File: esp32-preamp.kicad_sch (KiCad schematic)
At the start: 51 parts, among them J1 PWR IN, J10 TSOP382, J11 SELECT, J2 OUT, J3 LFE, J4 INPUT 1, J5 INPUT 2, J6 INPUT 2, J7 AMP PWR, J8 POT MOTOR, J9 VOLUME, Q1 2N3904, Q2 2N3904, Q3 2N3904, Q4 2N3904, U1 ESP32 D1 Mini, U2 TSR0.5-2450, U3 TPS60402DBV, U4 TPS72301DBV

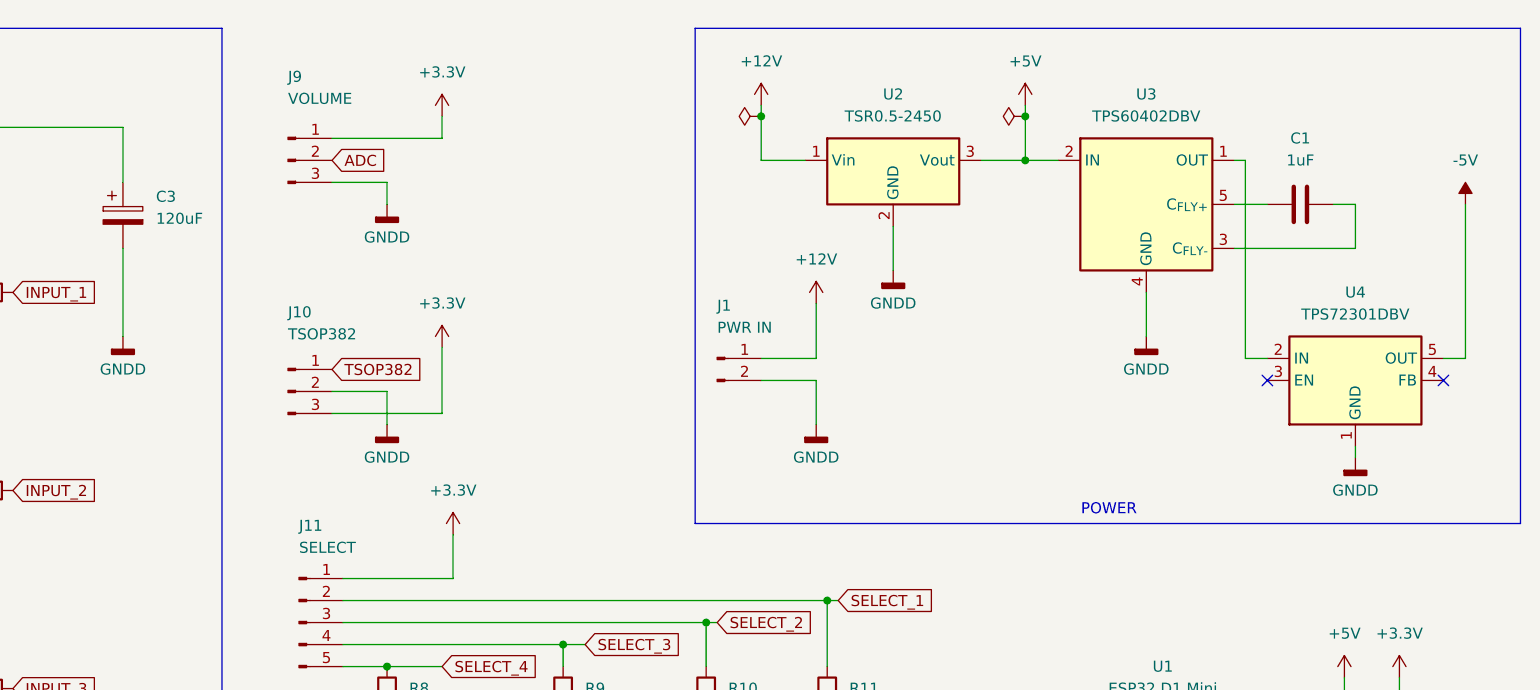
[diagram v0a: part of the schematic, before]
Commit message: Add caps on LDO
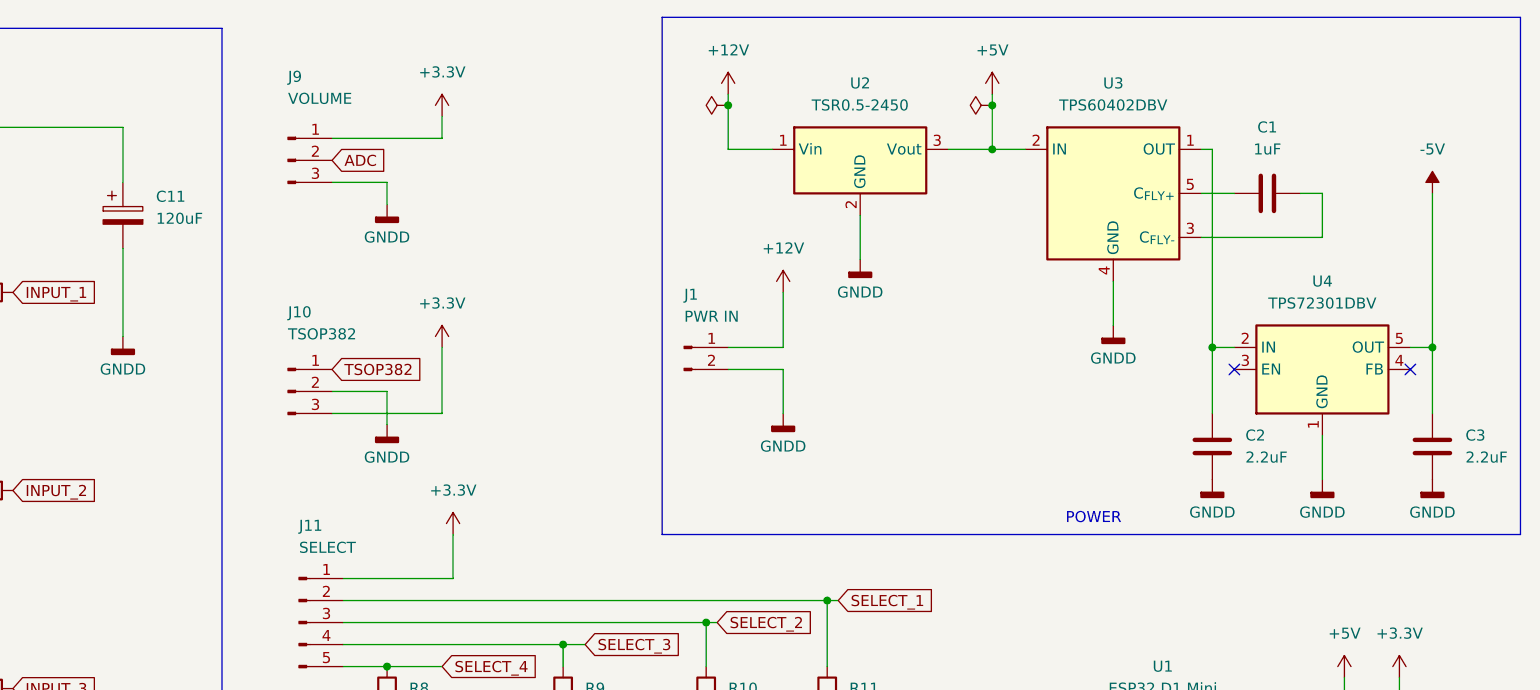
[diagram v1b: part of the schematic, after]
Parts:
- added C2, C3: 2.2uF, symbol Device:C
- renumbered C3 to C11
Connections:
- net -5V: now also C3.1
- net GNDD: now also C3.2
- net at U3.1 (OUT), U4.2 (IN): now also C2.1
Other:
- moved on the sheet: C1, J1, U2, U3, U4

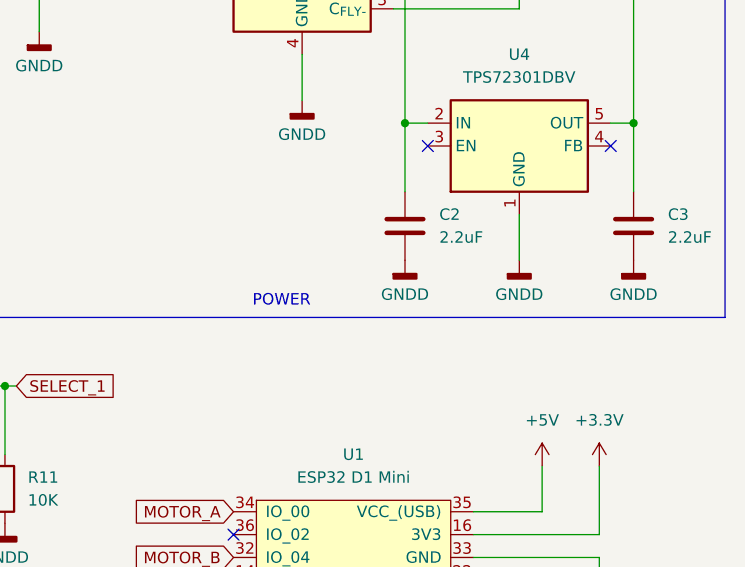
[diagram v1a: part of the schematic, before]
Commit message: Update esp32-preamp.kicad_sch
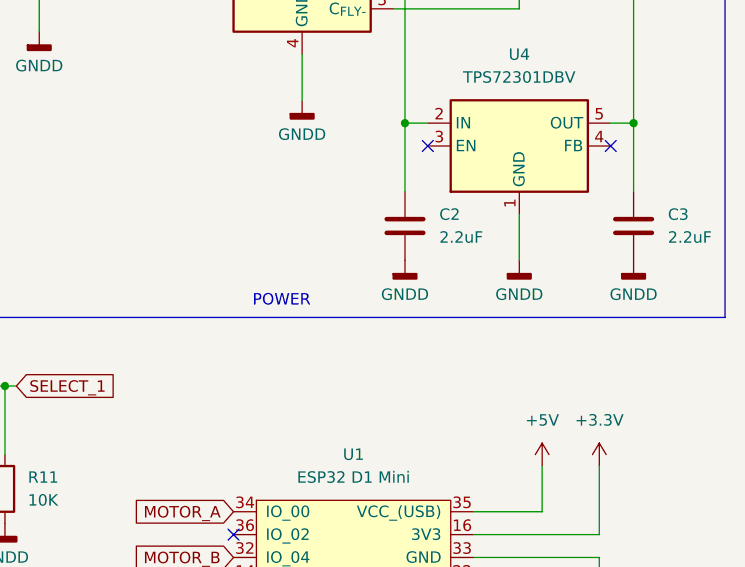
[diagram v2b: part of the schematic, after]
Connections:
- net GNDD: now also C2.2
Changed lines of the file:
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@@
 	(symbol
 		(lib_id "power:GNDD")
-		(at 247.65 67.3042 0)
+		(at 247.65 67.31 0)
 		(unit 1)
 		(body_style 1)
@@
 		(fields_autoplaced yes)
 		(property "Reference" "#PWR013"
-			(at 247.65 73.6542 0)
+			(at 247.65 73.66 0)
 			(hide yes)
 			(show_name no)
@@
 		)
 		(property "Value" "GNDD"
-			(at 247.65 71.1142 0)
+			(at 247.65 71.12 0)
 			(show_name no)
 			(do_not_autoplace no)
@@
 		)
 		(property "Footprint" ""
-			(at 247.65 67.3042 0)
+			(at 247.65 67.31 0)
 			(hide yes)
 			(show_name no)
@@
 		)
 		(property "Datasheet" ""
-			(at 247.65 67.3042 0)
+			(at 247.65 67.31 0)
 			(hide yes)
 			(show_name no)
@@
 		)
 		(property "Description" "Power symbol creates a global label with name \"GNDD\" , digital ground"
-			(at 247.65 67.3042 0)
+			(at 247.65 67.31 0)
 			(hide yes)
 			(show_name no)

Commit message: Milestone
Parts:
- removed J1: PWR IN, symbol Connector:Conn_01x02_Pin
- removed U2: TSR0.5-2450, Converter_DCDC:Converter_DCDC_TRACO_TSR0.5-24xx_TSR0.5-24xxx_THT, symbol Converter_DCDC:TSR0.5-2450
- added C9: 1uF, symbol Device:C
- added J9: PWR IN, symbol Connector:Conn_01x02_Pin
- added U3: TSR0.5-2450, Converter_DCDC:Converter_DCDC_TRACO_TSR0.5-24xx_TSR0.5-24xxx_THT, symbol Converter_DCDC:TSR0.5-2450
- added U4: TLV702475DBV, Package_TO_SOT_SMD:SOT-23-5_HandSoldering, symbol Regulator_Linear:TLV702475_SOT23-5
- renumbered C4 to C1, C2 to C10, C1 to C11, C3 to C12, C5 to C2, C6 to C3, C7 to C4, C8 to C5, C9 to C6, C11 to C7, C10 to C8, FB2 to FB1, FB1 to FB2, J4 to J1, J3 to J10, J2 to J11, J5 to J2, J6 to J3, J7 to J4, J9 to J5, J10 to J6, J11 to J7, R8 to R7, R7 to R8, U5 to U1, U6 to U2, U3 to U5, U1 to U6, U4 to U7
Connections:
- net +12V: now also J9.1 (Pin_1), U3.1 (Vin)
- net GNDA: now also C12.2, C9.1
- net GNDD: now also J9.2 (Pin_2), U3.2 (GND), U4.2 (GND); no longer C12.2
- net +5V renamed +5VD
- net +5VD: now also U3.3 (Vout), U4.1 (IN), U4.3 (EN); no longer C3.1, C4.1, U1.12 (+5V_A)
- net -5V renamed -5VA
- new net +5VA: C3.1, C4.1, C9.2, U1.12 (+5V_A), U4.5 (OUT)

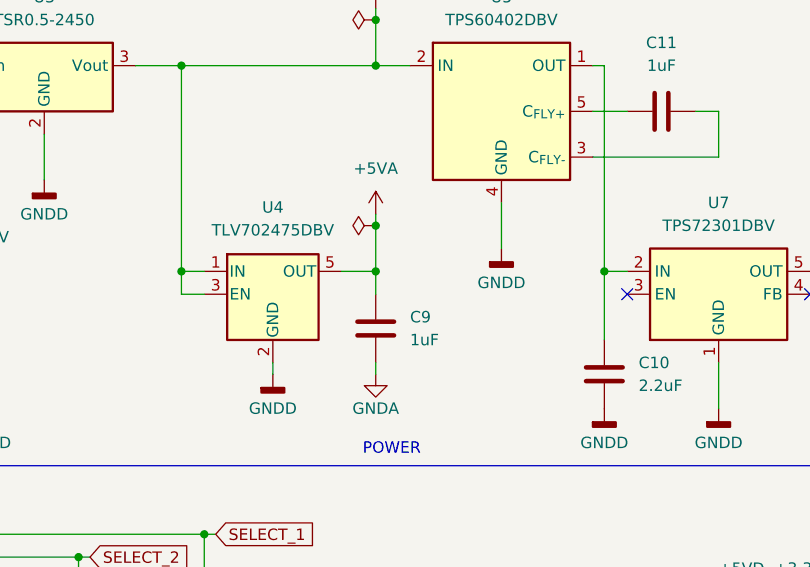
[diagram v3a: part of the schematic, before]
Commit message: Update esp32-preamp.kicad_sch
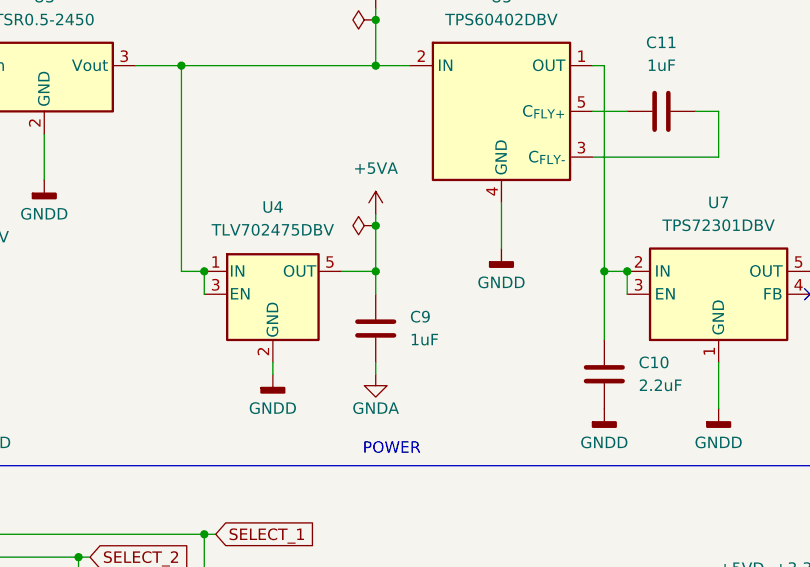
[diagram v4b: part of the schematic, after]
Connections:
- net at C10.1, U5.1 (OUT), U7.2 (IN): now also U7.3 (EN)
- no-connect marks 21 -> 20

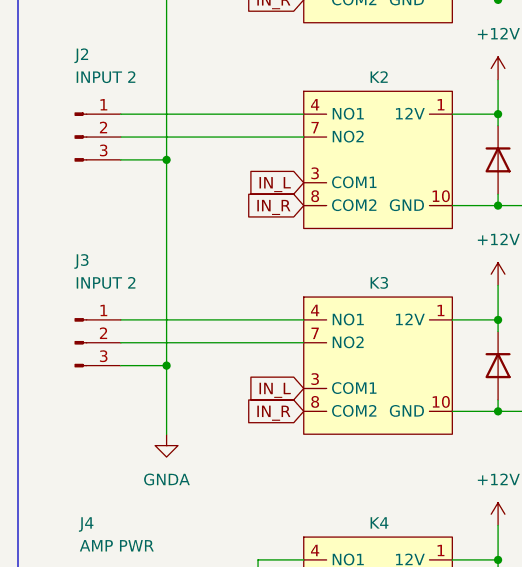
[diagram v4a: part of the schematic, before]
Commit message: Assign footprints
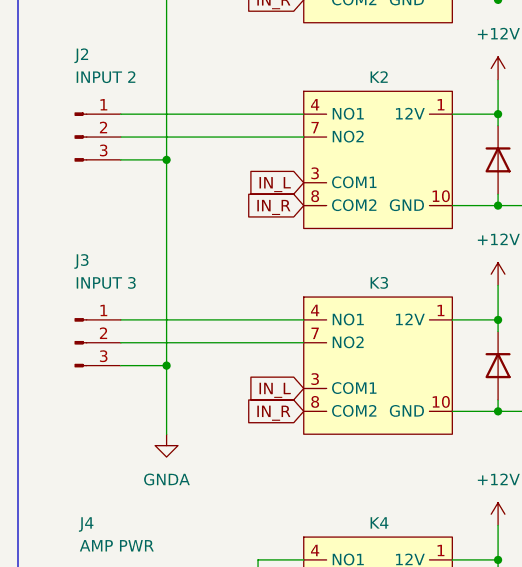
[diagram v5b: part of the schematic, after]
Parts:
- C1, C7, C8: footprint (none) -> Capacitor_THT:C_Radial_D4.0mm_H5.0mm_P1.50mm
- C10, C11, C12, C2, C3, C4, C5, C6, C9, FB1, FB2: footprint (none) -> Capacitor_SMD:C_1206_3216Metric_Pad1.33x1.80mm_HandSolder
- J1, J11, J2, J5, J6: footprint (none) -> Connector_JST:JST_XH_B3B-XH-A_1x03_P2.50mm_Vertical
- J10, J4, J8, J9: footprint (none) -> Connector_JST:JST_XH_B2B-XH-A_1x02_P2.50mm_Vertical
- J3: value INPUT 2 -> INPUT 3; footprint (none) -> Connector_JST:JST_XH_B3B-XH-A_1x03_P2.50mm_Vertical
- J7: footprint (none) -> Connector_JST:JST_XH_B5B-XH-A_1x05_P2.50mm_Vertical
- K1, K2, K3, K4: footprint (none) -> Panasonic TQ2:RELAY_TQ2_PAN
- R1, R10, R11, R2, R3, R4, R5, R6, R7, R8, R9: footprint (none) -> Resistor_SMD:R_1206_3216Metric_Pad1.30x1.75mm_HandSolder
- U1: footprint (none) -> footprints:DW16
- U2: footprint (none) -> Package_DIP:DIP-8_W7.62mm_Socket
- U6: footprint esp32-wemos-d1-mini:esp32-wemos-d1-mini -> ESP32 D1 Mini:esp32-wemos-d1-mini
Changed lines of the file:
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@@
 			)
 		)
-		(property "Footprint" ""
+		(property "Footprint" "Capacitor_SMD:C_1206_3216Metric_Pad1.33x1.80mm_HandSolder"
 			(at 214.63 121.412 90)
 			(hide yes)
@@
 			)
 		)
-		(property "Footprint" ""
+		(property "Footprint" "Resistor_SMD:R_1206_3216Metric_Pad1.30x1.75mm_HandSolder"
 			(at 138.43 165.608 90)
 			(hide yes)
@@
 			)
 		)
-		(property "Footprint" ""
+		(property "Footprint" "Panasonic TQ2:RELAY_TQ2_PAN"
 			(at 59.69 24.13 0)
 			(hide yes)
@@
 			)
 		)
-		(property "Footprint" ""
+		(property "Footprint" "Panasonic TQ2:RELAY_TQ2_PAN"
 			(at 59.69 69.85 0)
 			(hide yes)
@@
 			)
 		)
-		(property "Footprint" ""
+		(property "Footprint" "Resistor_SMD:R_1206_3216Metric_Pad1.30x1.75mm_HandSolder"
 			(at 105.41 116.332 90)
 			(hide yes)
@@
 			)
 		)
-		(property "Footprint" ""
+		(property "Footprint" "Connector_JST:JST_XH_B2B-XH-A_1x02_P2.50mm_Vertical"
 			(at 170.18 166.37 0)
 			(hide yes)
@@
 			)
 		)
-		(property "Footprint" ""
+		(property "Footprint" "Capacitor_SMD:C_1206_3216Metric_Pad1.33x1.80mm_HandSolder"
 			(at 274.0152 67.31 0)
 			(hide yes)
@@
 			)
 		)
-		(property "Footprint" ""
+		(property "Footprint" "Capacitor_SMD:C_1206_3216Metric_Pad1.33x1.80mm_HandSolder"
 			(at 83.5152 162.56 0)
 			(hide yes)
@@
 			)
 		)
-		(property "Footprint" ""
+		(property "Footprint" "Capacitor_SMD:C_1206_3216Metric_Pad1.33x1.80mm_HandSolder"
 			(at 214.63 146.812 90)
 			(hide yes)
@@
 			)
 		)
-		(property "Footprint" ""
+		(property "Footprint" "Connector_JST:JST_XH_B3B-XH-A_1x03_P2.50mm_Vertical"
 			(at 140.97 57.15 0)
 			(hide yes)
@@
 			)
 		)
-		(property "Value" "INPUT 2"
+		(property "Value" "INPUT 3"
 			(at 25.4 68.326 0)
 			(show_name no)
@@
 			)
 		)
-		(property "Footprint" ""
+		(property "Footprint" "Connector_JST:JST_XH_B3B-XH-A_1x03_P2.50mm_Vertical"
 			(at 25.4 74.93 0)
 			(hide yes)
@@
 			)
 		)
-		(property "Footprint" ""
+		(property "Footprint" "footprints:DW16"
 			(at 58.42 147.32 0)
 			(hide yes)
@@
 			)
 		)
-		(property "Footprint" ""
+		(property "Footprint" "Capacitor_THT:C_Radial_D4.0mm_H5.0mm_P1.50mm"
 			(at 122.8852 40.64 0)
 			(hide yes)
@@
 			)
 		)
-		(property "Footprint" ""
+		(property "Footprint" "Package_DIP:DIP-8_W7.62mm_Socket"
 			(at 168.91 107.95 0)
 			(hide yes)
@@
 			)
 		)
-		(property "Footprint" ""
+		(property "Footprint" "Capacitor_SMD:C_1206_3216Metric_Pad1.33x1.80mm_HandSolder"
 			(at 36.5252 161.29 0)
 			(hide yes)
@@
 			)
 		)
-		(property "Footprint" ""
+		(property "Footprint" "Capacitor_SMD:C_1206_3216Metric_Pad1.33x1.80mm_HandSolder"
 			(at 108.9152 162.56 0)
 			(hide yes)
@@
 			)
 		)
-		(property "Footprint" ""
+		(property "Footprint" "Connector_JST:JST_XH_B3B-XH-A_1x03_P2.50mm_Vertical"
 			(at 25.4 52.07 0)
 			(hide yes)
@@
 			)
 		)
-		(property "Footprint" ""
+		(property "Footprint" "Capacitor_SMD:C_1206_3216Metric_Pad1.33x1.80mm_HandSolder"
 			(at 221.2848 54.61 0)
 			(hide yes)
@@
 			)
 		)
-		(property "Footprint" ""
+		(property "Footprint" "Resistor_SMD:R_1206_3216Metric_Pad1.30x1.75mm_HandSolder"
 			(at 138.43 173.228 90)
 			(hide yes)
@@
 			)
 		)
-		(property "Footprint" ""
+		(property "Footprint" "Resistor_SMD:R_1206_3216Metric_Pad1.30x1.75mm_HandSolder"
 			(at 187.452 92.71 90)
 			(hide yes)
@@
 			)
 		)
-		(property "Footprint" ""
+		(property "Footprint" "Connector_JST:JST_XH_B2B-XH-A_1x02_P2.50mm_Vertical"
 			(at 167.64 59.69 0)
 			(hide yes)
@@
 			)
 		)
-		(property "Footprint" ""
+		(property "Footprint" "Capacitor_SMD:C_1206_3216Metric_Pad1.33x1.80mm_HandSolder"
 			(at 248.6152 67.31 0)
 			(hide yes)
@@
 			)
 		)
-		(property "Footprint" ""
+		(property "Footprint" "Capacitor_SMD:C_1206_3216Metric_Pad1.33x1.80mm_HandSolder"
 			(at 121.6152 162.56 0)
 			(hide yes)
@@
 			)
 		)
-		(property "Footprint" ""
+		(property "Footprint" "Capacitor_SMD:C_1206_3216Metric_Pad1.33x1.80mm_HandSolder"
 			(at 257.81 33.3248 0)
 			(hide yes)
@@
 			)
 		)
-		(property "Footprint" ""
+		(property "Footprint" "Capacitor_THT:C_Radial_D4.0mm_H5.0mm_P1.50mm"
 			(at 194.0052 125.73 0)
 			(hide yes)
@@
 			)
 		)
-		(property "Footprint" ""
+		(property "Footprint" "Capacitor_THT:C_Radial_D4.0mm_H5.0mm_P1.50mm"
 			(at 23.8252 161.29 0)
 			(hide yes)
@@
 			)
 		)
-		(property "Footprint" ""
+		(property "Footprint" "Resistor_SMD:R_1206_3216Metric_Pad1.30x1.75mm_HandSolder"
 			(at 150.622 92.71 90)
 			(hide yes)
@@
 			)
 		)
-		(property "Footprint" ""
+		(property "Footprint" "Resistor_SMD:R_1206_3216Metric_Pad1.30x1.75mm_HandSolder"
 			(at 170.942 92.71 90)
 			(hide yes)
@@
 			)
 		)
-		(property "Footprint" ""
+		(property "Footprint" "Connector_JST:JST_XH_B5B-XH-A_1x05_P2.50mm_Vertical"
 			(at 142.24 83.82 0)
 			(hide yes)
@@
 			)
 		)
-		(property "Footprint" ""
+		(property "Footprint" "Capacitor_SMD:C_1206_3216Metric_Pad1.33x1.80mm_HandSolder"
 			(at 96.2152 162.56 0)
 			(hide yes)
@@
 			)
 		)
-		(property "Footprint" ""
+		(property "Footprint" "Connector_JST:JST_XH_B2B-XH-A_1x02_P2.50mm_Vertical"
 			(at 25.4 101.6 0)
 			(hide yes)
@@
 			)
 		)
-		(property "Footprint" ""
+		(property "Footprint" "Panasonic TQ2:RELAY_TQ2_PAN"
 			(at 59.69 96.52 0)
 			(hide yes)
@@
 			)
 		)
-		(property "Footprint" "esp32-wemos-d1-mini:esp32-wemos-d1-mini"
+		(property "Footprint" "ESP32 D1 Mini:esp32-wemos-d1-mini"
 			(at 245.11 90.17 0)
 			(hide yes)
@@
 			)
 		)
-		(property "Footprint" ""
+		(property "Footprint" "Connector_JST:JST_XH_B3B-XH-A_1x03_P2.50mm_Vertical"
 			(at 25.4 29.21 0)
 			(hide yes)
@@
 			)
 		)
-		(property "Footprint" ""
+		(property "Footprint" "Resistor_SMD:R_1206_3216Metric_Pad1.30x1.75mm_HandSolder"
 			(at 105.41 66.802 90)
 			(hide yes)
@@
 			)
 		)
-		(property "Footprint" ""
+		(property "Footprint" "Connector_JST:JST_XH_B2B-XH-A_1x02_P2.50mm_Vertical"
 			(at 148.59 114.3 0)
 			(hide yes)
@@
 			)
 		)
-		(property "Footprint" ""
+		(property "Footprint" "Resistor_SMD:R_1206_3216Metric_Pad1.30x1.75mm_HandSolder"
 			(at 105.41 43.942 90)
 			(hide yes)
@@
 			)
 		)
-		(property "Footprint" ""
+		(property "Footprint" "Connector_JST:JST_XH_B3B-XH-A_1x03_P2.50mm_Vertical"
 			(at 140.97 30.48 0)
 			(hide yes)
@@
 			)
 		)
-		(property "Footprint" ""
+		(property "Footprint" "Resistor_SMD:R_1206_3216Metric_Pad1.30x1.75mm_HandSolder"
 			(at 105.41 89.662 90)
 			(hide yes)
@@
 			)
 		)
-		(property "Footprint" ""
+		(property "Footprint" "Resistor_SMD:R_1206_3216Metric_Pad1.30x1.75mm_HandSolder"
 			(at 152.4 146.558 90)
 			(hide yes)
@@
 			)
 		)
-		(property "Footprint" ""
+		(property "Footprint" "Resistor_SMD:R_1206_3216Metric_Pad1.30x1.75mm_HandSolder"
 			(at 201.422 92.71 90)
 			(hide yes)
@@
 			)
 		)
-		(property "Footprint" ""
+		(property "Footprint" "Connector_JST:JST_XH_B3B-XH-A_1x03_P2.50mm_Vertical"
 			(at 170.18 179.07 0)
 			(hide yes)
@@
 			)
 		)
-		(property "Footprint" ""
+		(property "Footprint" "Panasonic TQ2:RELAY_TQ2_PAN"
 			(at 59.69 46.99 0)
 			(hide yes)

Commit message: Tidy footprints
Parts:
- R5, R6: footprint Resistor_SMD:R_1206_3216Metric_Pad1.30x1.75mm_HandSolder -> Resistor_THT:R_Axial_Power_L20.0mm_W6.4mm_P22.40mm
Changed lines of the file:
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@@
 			)
 		)
-		(property "Footprint" "Resistor_SMD:R_1206_3216Metric_Pad1.30x1.75mm_HandSolder"
+		(property "Footprint" "Resistor_THT:R_Axial_Power_L20.0mm_W6.4mm_P22.40mm"
 			(at 138.43 165.608 90)
 			(hide yes)
@@
 			)
 		)
-		(property "Footprint" "Resistor_SMD:R_1206_3216Metric_Pad1.30x1.75mm_HandSolder"
+		(property "Footprint" "Resistor_THT:R_Axial_Power_L20.0mm_W6.4mm_P22.40mm"
 			(at 138.43 173.228 90)
 			(hide yes)

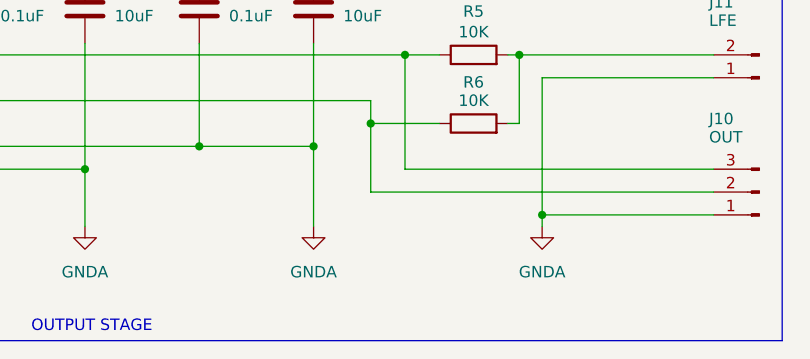
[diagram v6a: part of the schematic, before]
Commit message: Fix R5/R6 footprint
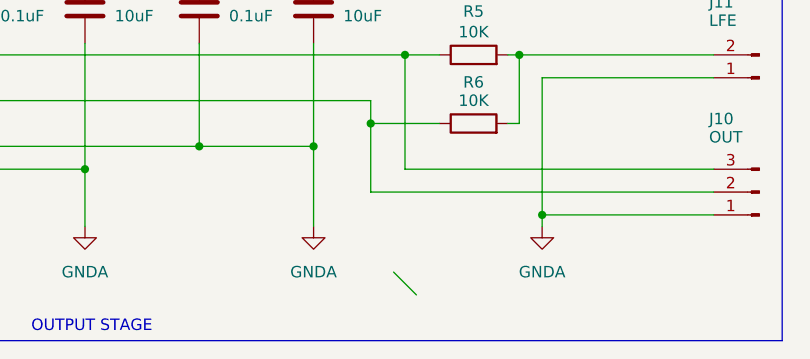
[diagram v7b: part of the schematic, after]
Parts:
- R5, R6: footprint Resistor_THT:R_Axial_Power_L20.0mm_W6.4mm_P22.40mm -> Resistor_THT:R_Axial_Power_L38.0mm_W9.0mm_P40.64mm
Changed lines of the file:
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@@
 		(at 255.27 120.65)
 	)
+	(bus_entry
+		(at 129.54 187.96)
+		(size 2.54 2.54)
+		(stroke
+			(width 0)
+			(type default)
+		)
+	)
 	(wire
 		(pts
@@
 			)
 		)
-		(property "Footprint" "Resistor_THT:R_Axial_Power_L20.0mm_W6.4mm_P22.40mm"
+		(property "Footprint" "Resistor_THT:R_Axial_Power_L38.0mm_W9.0mm_P40.64mm"
 			(at 138.43 165.608 90)
 			(hide yes)
@@
 			)
 		)
-		(property "Footprint" "Resistor_THT:R_Axial_Power_L20.0mm_W6.4mm_P22.40mm"
+		(property "Footprint" "Resistor_THT:R_Axial_Power_L38.0mm_W9.0mm_P40.64mm"
 			(at 138.43 173.228 90)
 			(hide yes)

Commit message: Group footprints
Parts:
- C6: footprint Capacitor_SMD:C_1206_3216Metric_Pad1.33x1.80mm_HandSolder -> Capacitor_THT:C_Radial_D4.0mm_H5.0mm_P1.50mm
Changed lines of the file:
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@@
 			)
 		)
-		(property "Footprint" "Capacitor_SMD:C_1206_3216Metric_Pad1.33x1.80mm_HandSolder"
+		(property "Footprint" "Capacitor_THT:C_Radial_D4.0mm_H5.0mm_P1.50mm"
 			(at 121.6152 162.56 0)
 			(hide yes)
